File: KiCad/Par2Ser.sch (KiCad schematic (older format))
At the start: 41 parts, among them J1 DB25_Male, J2 USB_C_Receptacle_USB2.0, J3 Conn_02x05_Odd_Even, U1 LC4032V-5TN48C, U2 FT240XS-R, U3 TLV75533PDBVR, Y1 SIT1534AI-H4-DCC-00.032

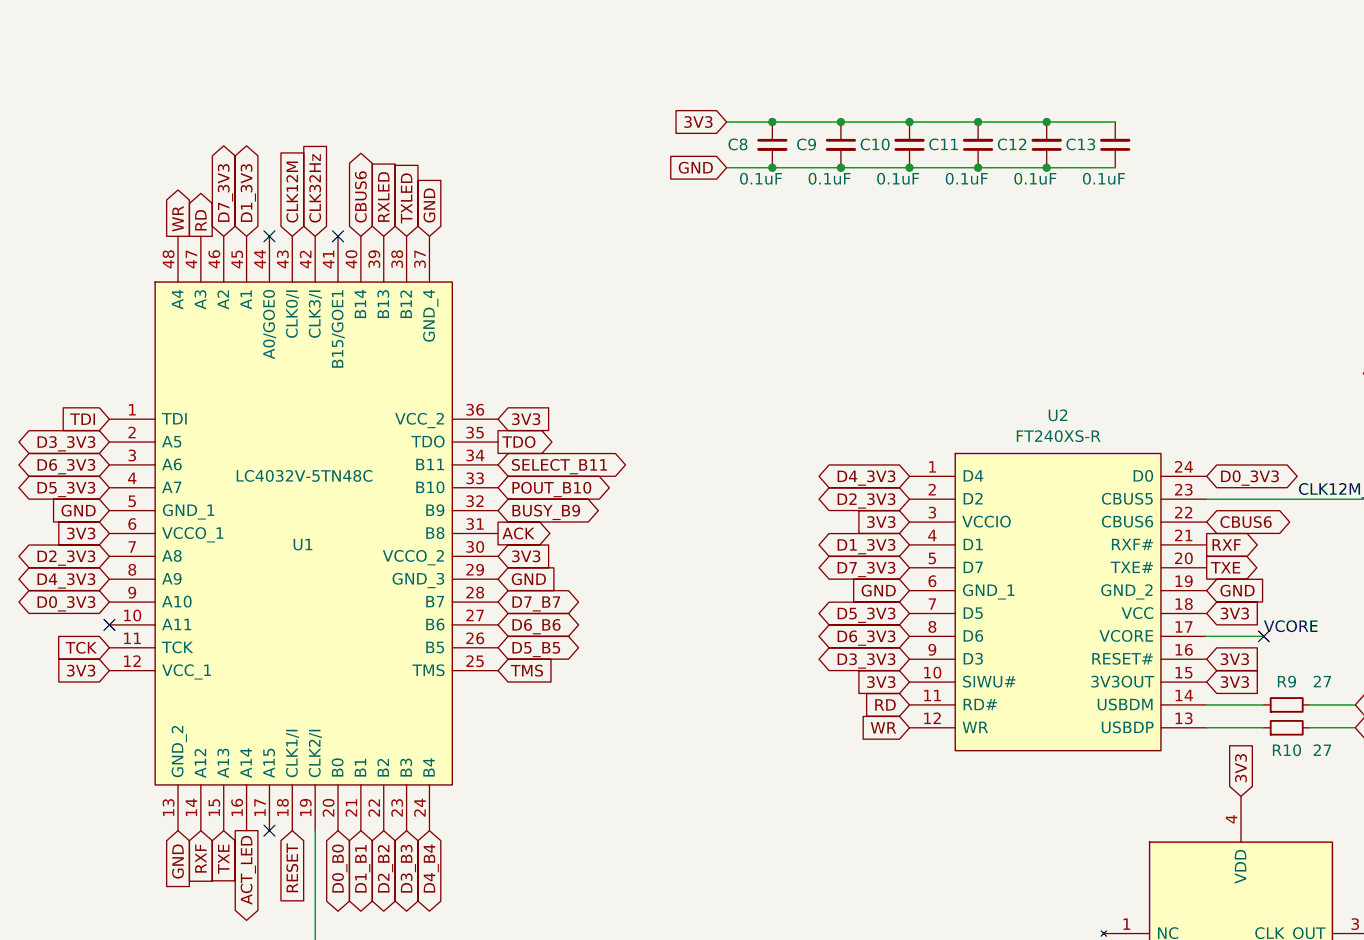
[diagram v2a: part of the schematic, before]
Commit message: Add decoupling cap and 3.3v supply to MEMS Oscillator
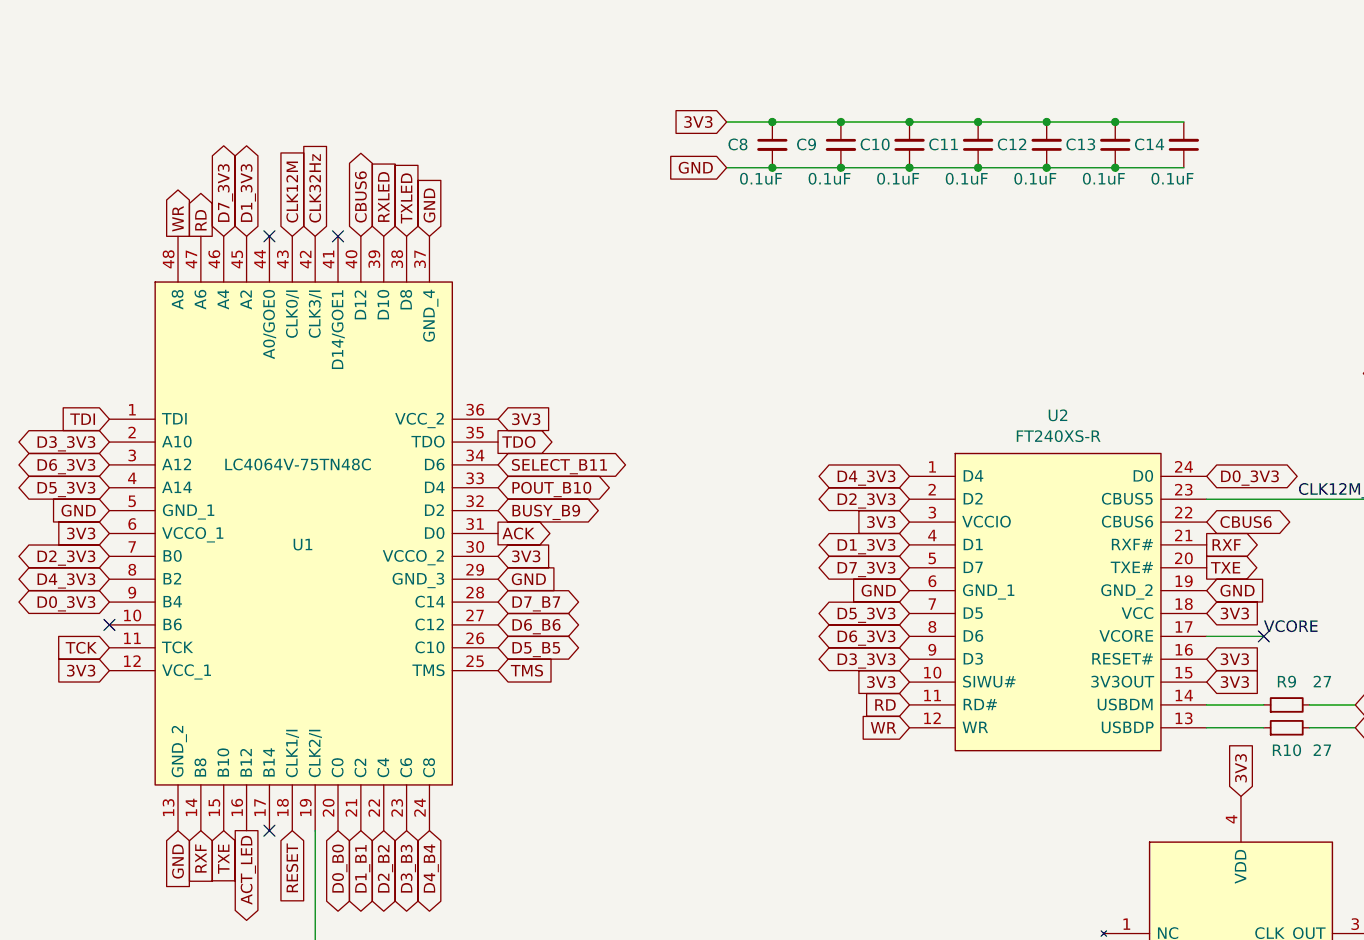
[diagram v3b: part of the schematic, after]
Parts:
- removed U1: LC4032V-5TN48C, Package_QFP:TQFP-48_7x7mm_P0.5mm, symbol Par2Ser:LC4032V-5TN48C
- added C14: 0.1uF, Capacitor_SMD:C_0603_1608Metric_Pad1.08x0.95mm_HandSolder, symbol Device:C_Small
- added U1: LC4064V-75TN48C, Package_QFP:TQFP-48_7x7mm_P0.5mm, symbol Par2Ser:LC4064V-75TN48C
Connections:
- net 3V3: now also C14.2, U1.12 (VCC_1), U1.30 (VCCO_2), U1.36 (VCC_2), U1.6 (VCCO_1)
- net ACK: now also U1.31 (D0)
- net ACT_LED: now also U1.16 (B12)
- net BUSY_B9: now also U1.32 (D2)
- net CBUS6: now also U1.40 (D12)
- net CLK12M: now also U1.43 (CLK0/I)
- net CLK32Hz: now also U1.42 (CLK3/I)
- net D0_3V3: now also U1.9 (B4)
- net D0_B0: now also U1.20 (C0)
- net D1_3V3: now also U1.45 (A2)
- net D1_B1: now also U1.21 (C2)
- net D2_3V3: now also U1.7 (B0)
- net D2_B2: now also U1.22 (C4)
- net D3_3V3: now also U1.2 (A10)
- net D3_B3: now also U1.23 (C6)
- net D4_3V3: now also U1.8 (B2)
- net D4_B4: now also U1.24 (C8)
- net D5_3V3: now also U1.4 (A14)
- net D5_B5: now also U1.26 (C10)
- net D6_3V3: now also U1.3 (A12)
- net D6_B6: now also U1.27 (C12)
- net D7_3V3: now also U1.46 (A4)
- net D7_B7: now also U1.28 (C14)
- net GND: now also C14.1, U1.13 (GND_2), U1.29 (GND_3), U1.37 (GND_4), U1.5 (GND_1)
- net POUT_B10: now also U1.33 (D4)
- net RD: now also U1.47 (A6)
- net RESET: now also U1.18 (CLK1/I)
- net RXF: now also U1.14 (B8)
- net RXLED: now also U1.39 (D10)
- net SELECT_B11: now also U1.34 (D6)
- net STRB: now also U1.19 (CLK2/I)
- net TCK: now also U1.11 (TCK)
- net TDI: now also U1.1 (TDI)
- net TDO: now also U1.35 (TDO)
- net TMS: now also U1.25 (TMS)
- net TXE: now also U1.15 (B10)
- net TXLED: now also U1.38 (D8)
- net WR: now also U1.48 (A8)
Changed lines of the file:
@@
-	1    0    0    -1
-$EndComp
-$Comp
-L Par2Ser:LC4032V-5TN48C U1
-U 1 1 6A10FE30
-P 5850 3000
-F 0 "U1" H 5800 3000 50  0000 L CNN
-F 1 "LC4032V-5TN48C" H 5550 3300 50  0000 L CNN
-F 2 "Package_QFP:TQFP-48_7x7mm_P0.5mm" H 6550 4150 50  0001 L CNN
-F 3 "https://componentsearchengine.com/Datasheets/34/LC4032V-5TN48C.pdf" H 6550 4050 50  0001 L CNN
-	1    5850 3000
 	1    0    0    -1
 $EndComp
@@
 	1    0    0    -1
 $EndComp
+$Comp
+L Par2Ser:LC4064V-75TN48C U1
+U 1 1 6A25C54A
+P 5850 3000
+F 0 "U1" H 5800 3000 50  0000 L CNN
+F 1 "LC4064V-75TN48C" H 5500 3350 50  0000 L CNN
+F 2 "Package_QFP:TQFP-48_7x7mm_P0.5mm" H 6550 4150 50  0001 L CNN
+F 3 "" H 6550 4050 50  0001 L CNN
+	1    5850 3000
+	1    0    0    -1
+$EndComp
+$Comp
+L Device:C_Small C14
+U 1 1 6A282A8C
+P 9700 1250
+F 0 "C14" H 9850 1250 50  0000 C CNN
+F 1 "0.1uF" H 9750 1400 50  0000 C CNN
+F 2 "Capacitor_SMD:C_0603_1608Metric_Pad1.08x0.95mm_HandSolder" H 9700 1250 50  0001 C CNN
+F 3 "~" H 9700 1250 50  0001 C CNN
+	1    9700 1250
+	-1   0    0    1
+$EndComp
+Wire Wire Line
+	9400 1150 9700 1150
+Connection ~ 9400 1150
+Wire Wire Line
+	9400 1350 9700 1350
+Connection ~ 9400 1350
 $EndSCHEMATC

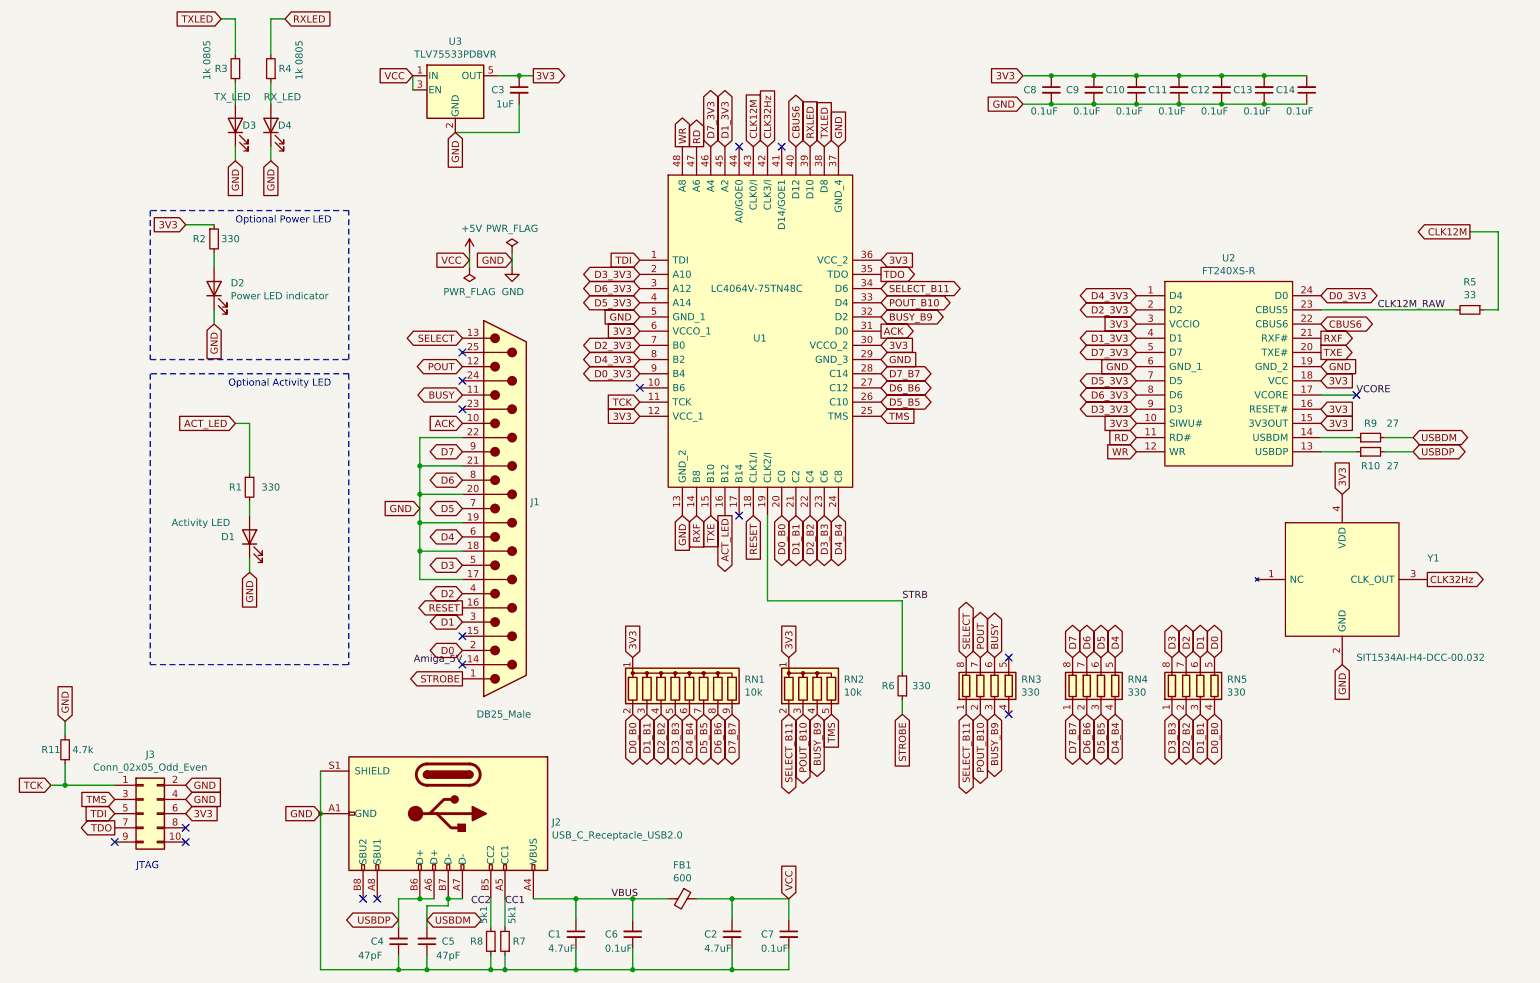
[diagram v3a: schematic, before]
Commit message: Remove SIT1534 (Y1) slow clock not needed
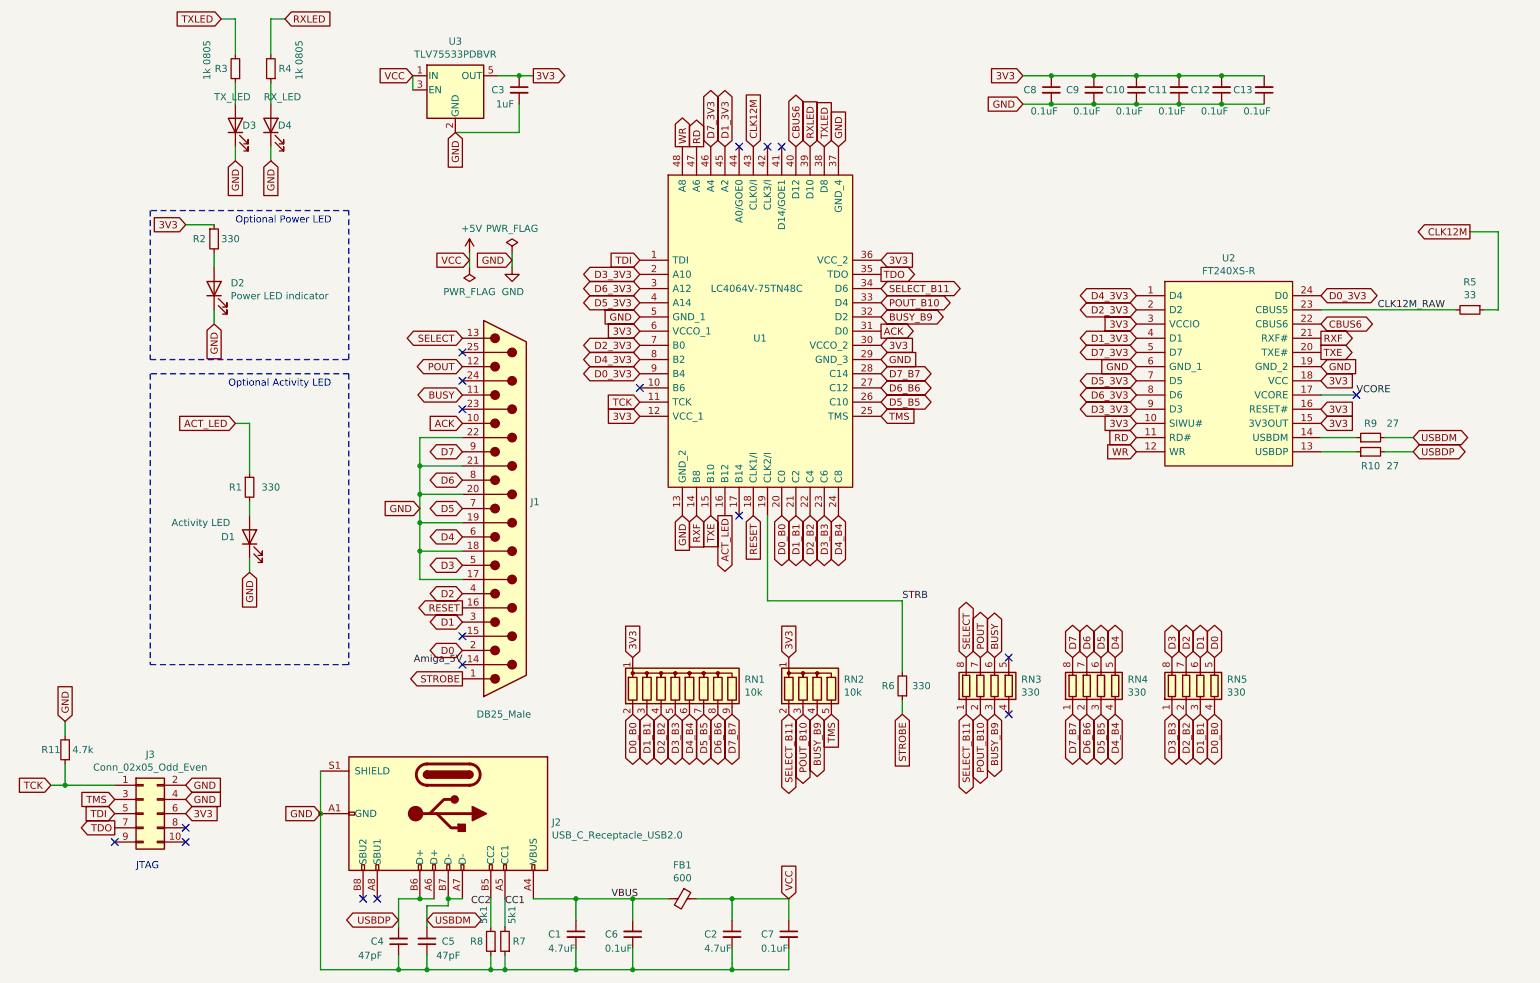
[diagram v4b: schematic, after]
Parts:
- removed C14: 0.1uF, Capacitor_SMD:C_0603_1608Metric_Pad1.08x0.95mm_HandSolder, symbol Device:C_Small
- removed Y1: SIT1534AI-H4-DCC-00.032, Par2Ser:SIT1534AIH4DCC00256, symbol Par2Ser:SIT1534AI-H4-DCC-00.032
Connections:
- net CLK32Hz: no longer names the net of U1.42 (CLK3/I)
- no-connect marks 17 -> 18
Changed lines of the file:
@@
 Wire Wire Line
 	4150 1550 4150 1350
-Text GLabel 5900 1650 1    50   Input ~ 0
-CLK32Hz
-Text GLabel 9950 5300 3    50   Input ~ 0
-GND
-Text GLabel 9950 4100 1    50   Input ~ 0
-3V3
-Text GLabel 10550 4700 2    50   Output ~ 0
-CLK32Hz
-$Comp
-L Par2Ser:SIT1534AI-H4-DCC-00.032 Y1
-U 1 1 6A21EC58
-P 9950 4700
-F 0 "Y1" H 10550 4850 50  0000 L CNN
-F 1 "SIT1534AI-H4-DCC-00.032" H 10050 4150 50  0000 L CNN
-F 2 "Par2Ser:SIT1534AIH4DCC00256" H 10400 5100 50  0001 L CNN
-F 3 "https://www.sitime.com/support/resource-library/datasheets/sit1534-datasheet" H 10400 5000 50  0001 L CNN
-	1    9950 4700
-	1    0    0    -1
-$EndComp
 $Comp
 L Par2Ser:LC4064V-75TN48C U1
@@
 	1    0    0    -1
 $EndComp
-$Comp
-L Device:C_Small C14
-U 1 1 6A282A8C
-P 9700 1250
-F 0 "C14" H 9850 1250 50  0000 C CNN
-F 1 "0.1uF" H 9750 1400 50  0000 C CNN
-F 2 "Capacitor_SMD:C_0603_1608Metric_Pad1.08x0.95mm_HandSolder" H 9700 1250 50  0001 C CNN
-F 3 "~" H 9700 1250 50  0001 C CNN
-	1    9700 1250
-	-1   0    0    1
-$EndComp
-Wire Wire Line
-	9400 1150 9700 1150
-Connection ~ 9400 1150
-Wire Wire Line
-	9400 1350 9700 1350
-Connection ~ 9400 1350
+NoConn ~ 5900 1650
 $EndSCHEMATC
